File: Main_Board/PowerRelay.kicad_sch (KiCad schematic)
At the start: 27 parts, among them J1 Screw_Terminal_01x03, J2 Conn_01x20_Female, J3 Conn_01x20_Female, J5 Screw_Terminal_01x03, J6 Screw_Terminal_01x03, J8 AudioJack4, K1 G5LE-1A4_DC3, K2 G5LE-1A4_DC3, Q1 2N7000, Q2 2N7000

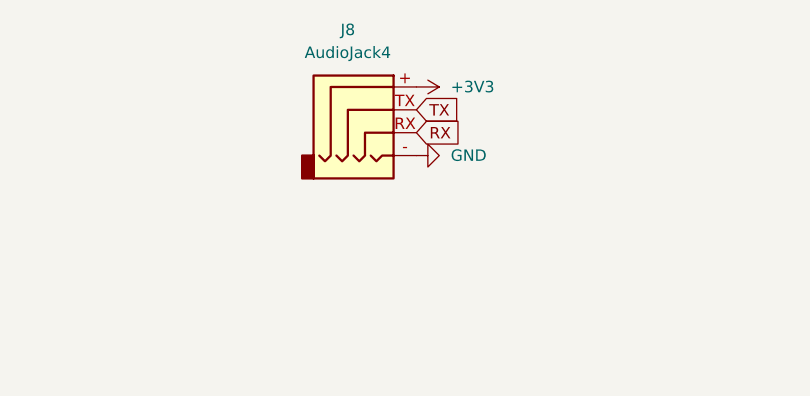
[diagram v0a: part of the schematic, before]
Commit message: change footprint for barrel connector
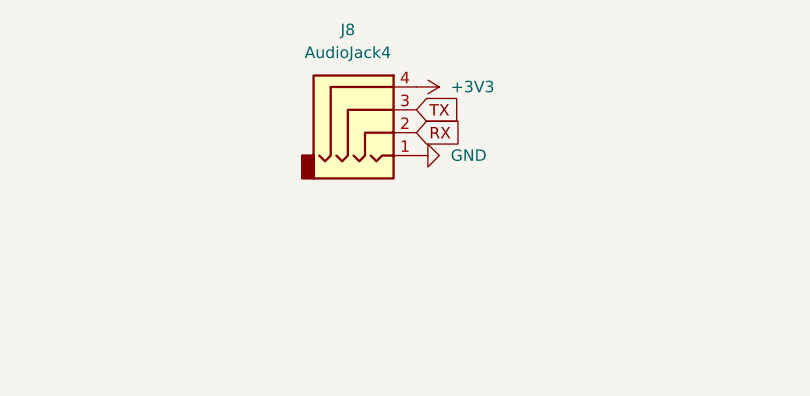
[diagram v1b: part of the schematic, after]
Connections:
- net +3V3: now also J8.4; no longer J8.+
- net GND: now also J8.1; no longer J8.-
- net RX: now also J8.2; no longer J8.RX
- net TX: now also J8.3; no longer J8.TX
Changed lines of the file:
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@@
       (effects (font (size 1.27 1.27)) hide)
     )
-    (pin "+")
-    (pin "-")
-    (pin "RX")
-    (pin "TX")
+    (pin "1")
+    (pin "2")
+    (pin "3")
+    (pin "4")
   )
   (symbol (lib_id "Mechanical:MountingHole") (at 297.18 156.21 0) (unit 1)

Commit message: multiple changes and convert to ki cad 7
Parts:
- removed H5: MountingHole, MountingHole:MountingHole_3mm, symbol Mechanical:MountingHole
- added F3: Fuse, 39105000000:39105000000, symbol Device:Fuse
- added J4: Conn_01x02_Female, Connector_PinHeader_2.54mm:PinHeader_1x02_P2.54mm_Vertical, symbol Connector:Conn_01x02_Female
- renumbered H6 to H5
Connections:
- net +3V3: now also J4.2 (Pin_2); no longer J8.4
- new net: F3.2, J4.1 (Pin_1)
- new net: F3.1, J8.4
